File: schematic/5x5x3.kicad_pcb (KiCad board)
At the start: 4 copper layers, 100 x 100 mm, 119 parts, among them J1 SW Debug, J2 Battery, SW11 SW, SW12 SW, SW13 SW, SW14 SW, SW21 SW, SW22 SW, SW23 SW, SW24 SW, SW25 SW, SW31 SW, SW32 SW, SW33 SW, SW34 SW, SW35 SW, SW41 SW, SW42 SW, SW43 SW, SW44 SW, SW45 SW, SW51 SW, SW52 SW, SW53 SW, SW54 SW, SW55 SW, SW6 ALPS_EC11, U1 nice_nano v2

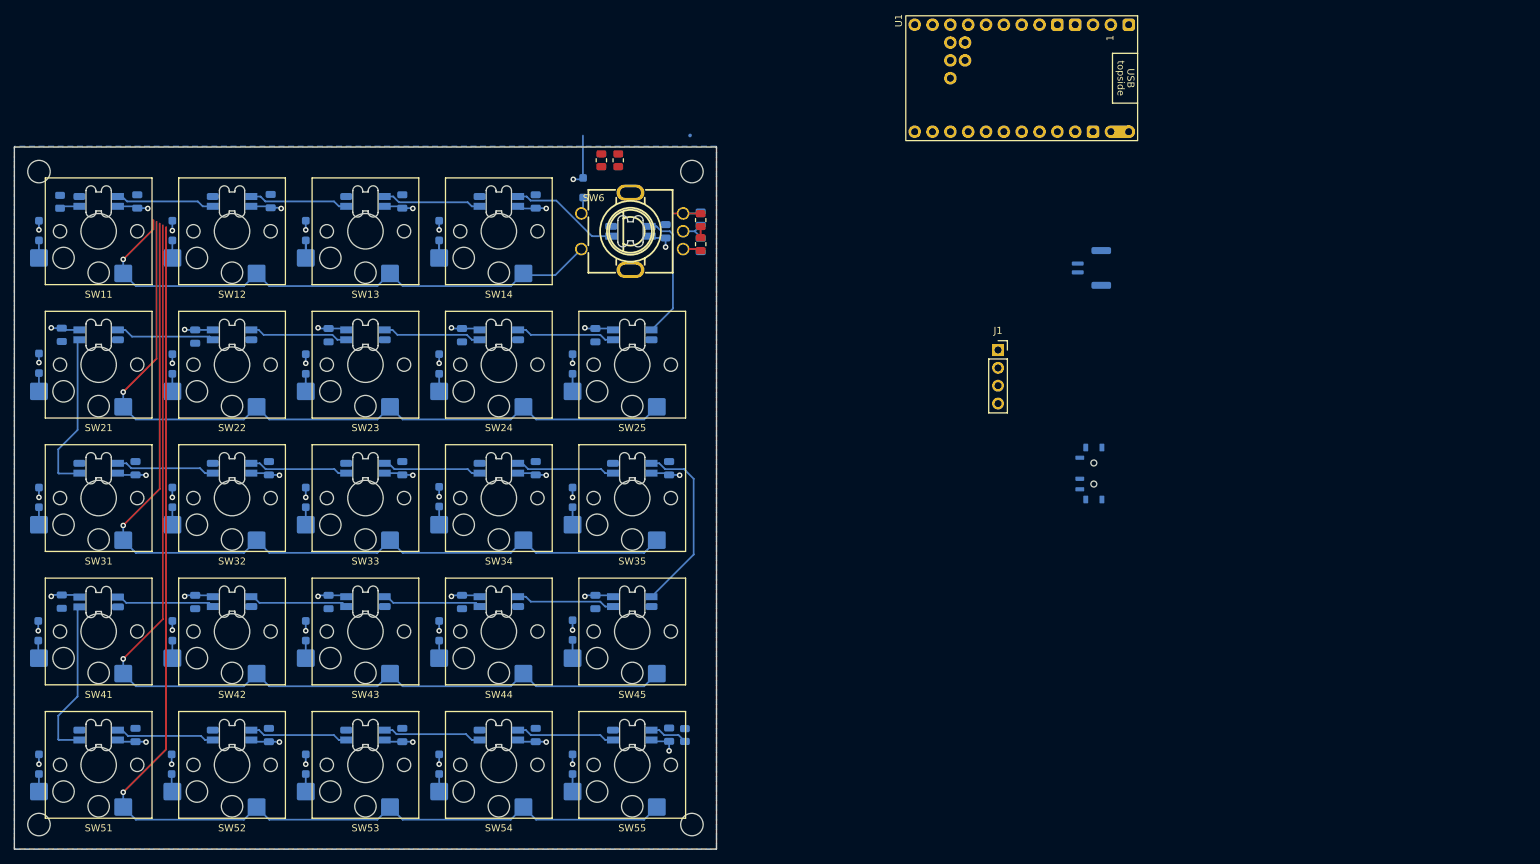
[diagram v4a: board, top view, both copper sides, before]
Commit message: Mapped 5x5x2 pins onto 5x5x3
But there is overlap, so some work is needed. Also, what rubbish am I
bringing in from the old file?
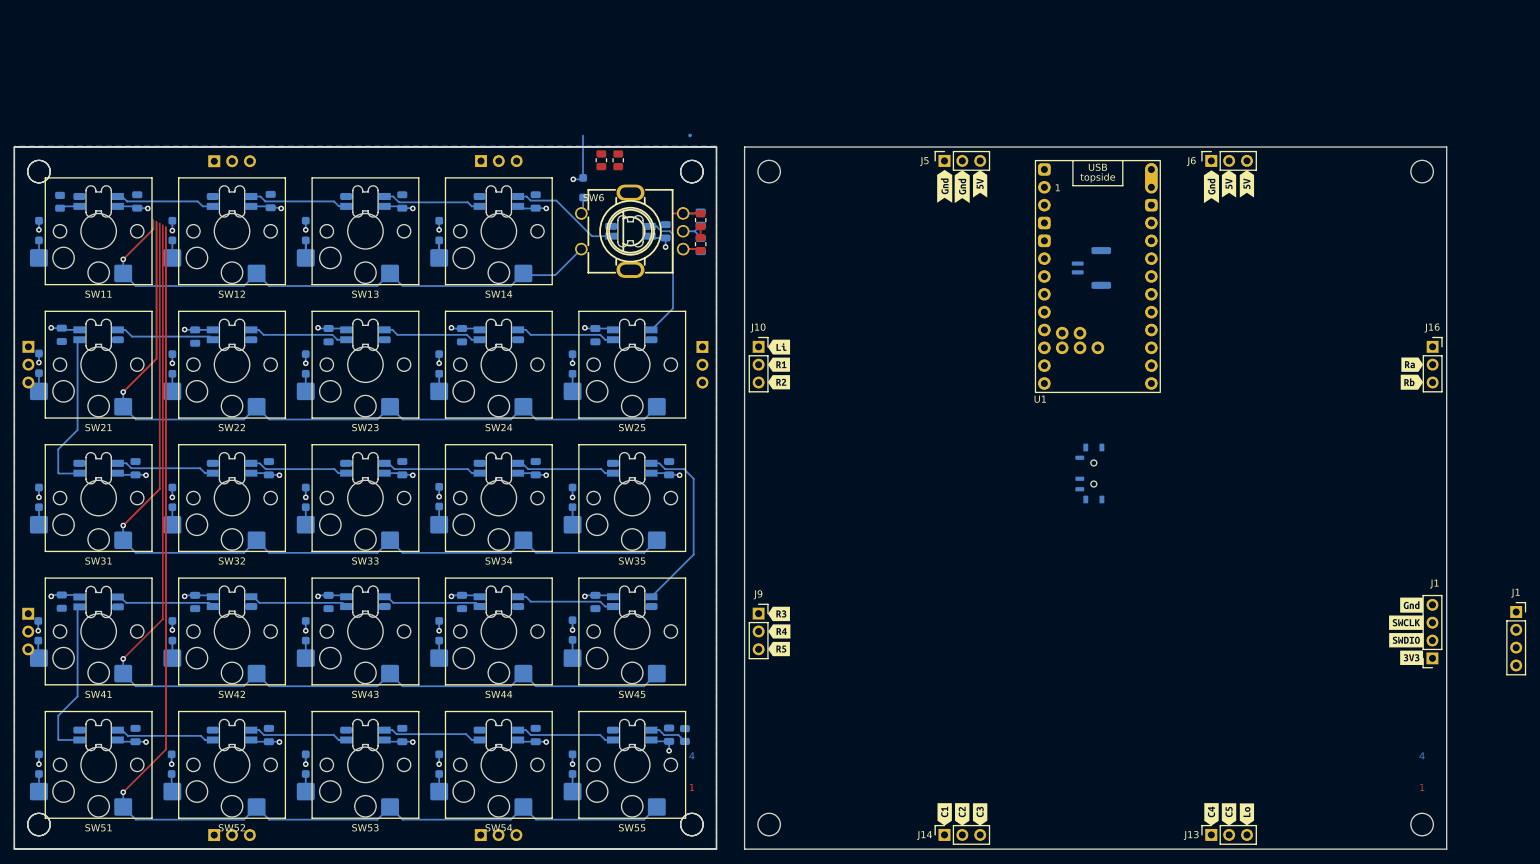
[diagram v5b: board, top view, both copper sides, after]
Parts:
- added G***: LOGO, LOGO, B.Cu at (86.0, 133.8)
- added G***: LOGO, LOGO, B.Cu at (190.0, 133.8)
- added J1: SW Debug, Connector_PinSocket_2.54mm:PinSocket_1x04_P2.54mm_Vertical, F.Cu at (238.0, 110.8)
- added J10: Conn_01x03_Female, Connector_PinSocket_2.54mm:PinSocket_1x03_P2.54mm_Vertical, F.Cu at (142.0, 66.5)
- added J11: Conn_01x03_Male, Connector_PinSocket_2.54mm:PinSocket_1x03_P2.54mm_Vertical, B.Cu at (102.4, 136.0)
- added J12: Conn_01x03_Male, Connector_PinSocket_2.54mm:PinSocket_1x03_P2.54mm_Vertical, B.Cu at (64.5, 136.0)
- added J13: Conn_01x03_Female, Connector_PinSocket_2.54mm:PinSocket_1x03_P2.54mm_Vertical, F.Cu at (206.5, 136.0)
- added J14: Conn_01x03_Female, Connector_PinSocket_2.54mm:PinSocket_1x03_P2.54mm_Vertical, F.Cu at (168.5, 136.0)
- added J15: Conn_01x03_Male, Connector_PinSocket_2.54mm:PinSocket_1x03_P2.54mm_Vertical, B.Cu at (134.0, 66.5)
- added J16: Conn_01x03_Female, Connector_PinSocket_2.54mm:PinSocket_1x03_P2.54mm_Vertical, F.Cu at (238.0, 66.5)
- added J3: Conn_01x03_Male, Connector_PinSocket_2.54mm:PinSocket_1x03_P2.54mm_Vertical, B.Cu at (64.5, 40.0)
- added J4: Conn_01x03_Male, Connector_PinSocket_2.54mm:PinSocket_1x03_P2.54mm_Vertical, B.Cu at (102.5, 40.0)
- added J5: Conn_01x03_Female, Connector_PinSocket_2.54mm:PinSocket_1x03_P2.54mm_Vertical, F.Cu at (168.5, 40.0)
- added J6: Conn_01x03_Female, Connector_PinSocket_2.54mm:PinSocket_1x03_P2.54mm_Vertical, F.Cu at (206.5, 40.0)
- added J7: Conn_01x03_Male, Connector_PinSocket_2.54mm:PinSocket_1x03_P2.54mm_Vertical, B.Cu at (38.0, 104.5)
- added J8: Conn_01x03_Male, Connector_PinSocket_2.54mm:PinSocket_1x03_P2.54mm_Vertical, B.Cu at (38.0, 66.5)
- added J9: Conn_01x03_Female, Connector_PinSocket_2.54mm:PinSocket_1x03_P2.54mm_Vertical, F.Cu at (142.0, 104.5)
- added REF**: MountingHole_3.2mm_M3, MountingHole:MountingHole_3.2mm_M3, F.Cu at (143.5, 41.5)
- added REF**: MountingHole_3.2mm_M3, MountingHole:MountingHole_3.2mm_M3, F.Cu at (132.5, 134.5)
- added REF**: MountingHole_3.2mm_M3, MountingHole:MountingHole_3.2mm_M3, F.Cu at (132.5, 41.5)
- added REF**: MountingHole_3.2mm_M3, MountingHole:MountingHole_3.2mm_M3, F.Cu at (39.5, 134.5)
- added REF**: MountingHole_3.2mm_M3, MountingHole:MountingHole_3.2mm_M3, F.Cu at (39.5, 41.5)
- added REF**: MountingHole_3.2mm_M3, MountingHole:MountingHole_3.2mm_M3, F.Cu at (236.5, 41.5)
- added REF**: MountingHole_3.2mm_M3, MountingHole:MountingHole_3.2mm_M3, F.Cu at (143.5, 134.5)
- added REF**: MountingHole_3.2mm_M3, MountingHole:MountingHole_3.2mm_M3, F.Cu at (236.5, 134.5)
- added kibuzzard-62AF6B0E: G***, kibuzzard-62AF6B0E, B.Cu at (38.0, 102.0)
- added kibuzzard-62AF6B38: G***, kibuzzard-62AF6B38, B.Cu at (40.5, 107.0)
- added kibuzzard-62AF6B38: G***, kibuzzard-62AF6B38, B.Cu at (145.0, 107.0)
- added kibuzzard-62AF6B7C: G***, kibuzzard-62AF6B7C, B.Cu at (145.0, 109.5)
- added kibuzzard-62AF6B7C: G***, kibuzzard-62AF6B7C, B.Cu at (40.5, 109.5)
- added kibuzzard-62AF6BA3: G***, kibuzzard-62AF6BA3, B.Cu at (145.0, 71.5)
- added kibuzzard-62AF6BA3: G***, kibuzzard-62AF6BA3, B.Cu at (40.5, 71.5)
- added kibuzzard-62AF6BAD: G***, kibuzzard-62AF6BAD, B.Cu at (145.0, 69.0)
- added kibuzzard-62AF6BAD: G***, kibuzzard-62AF6BAD, B.Cu at (40.5, 69.0)
- added kibuzzard-62AF6BF3: G***, kibuzzard-62AF6BF3, B.Cu at (38.0, 63.8)
- added kibuzzard-62AF6D1E: G***, kibuzzard-62AF6D1E, B.Cu at (72.5, 40.0)
- added kibuzzard-62AF6D1E: G***, kibuzzard-62AF6D1E, B.Cu at (110.5, 40.0)
- added kibuzzard-62AF6DB1: G***, kibuzzard-62AF6DB1, B.Cu at (99.0, 40.0)
- added kibuzzard-62AF6DB1: G***, kibuzzard-62AF6DB1, B.Cu at (61.0, 40.0)
- added kibuzzard-62AF6E15: G***, kibuzzard-62AF6E15, B.Cu at (131.5, 69.0)
- added kibuzzard-62AF6E21: G***, kibuzzard-62AF6E21, B.Cu at (131.5, 71.5)
- added kibuzzard-62AF6EB6: G***, kibuzzard-62AF6EB6, B.Cu at (99.8, 136.0)
- added kibuzzard-62AF6EDD: G***, kibuzzard-62AF6EDD, B.Cu at (62.0, 136.0)
- added kibuzzard-62AF6F00: G***, kibuzzard-62AF6F00, B.Cu at (72.2, 136.0)
- added kibuzzard-62AF6F11: G***, kibuzzard-62AF6F11, B.Cu at (110.0, 136.0)
- added kibuzzard-62AF73B1: G***, kibuzzard-62AF73B1, F.Cu at (206.5, 43.6)
- added kibuzzard-62AF73B1: G***, kibuzzard-62AF73B1, F.Cu at (171.0, 43.6)
- added kibuzzard-62AF73B1: G***, kibuzzard-62AF73B1, F.Cu at (168.5, 43.6)
- added kibuzzard-62AF73B1: G***, kibuzzard-62AF73B1, B.Cu at (206.5, 43.8)
- added kibuzzard-62AF73B1: G***, kibuzzard-62AF73B1, B.Cu at (171.0, 43.8)
- added kibuzzard-62AF73B1: G***, kibuzzard-62AF73B1, B.Cu at (168.5, 43.8)
- added kibuzzard-62AF73D1: G***, kibuzzard-62AF73D1, F.Cu at (209.0, 43.2)
- added kibuzzard-62AF73D1: G***, kibuzzard-62AF73D1, F.Cu at (173.6, 43.2)
- added kibuzzard-62AF73D1: G***, kibuzzard-62AF73D1, F.Cu at (211.6, 43.2)
- added kibuzzard-62AF73D1: G***, kibuzzard-62AF73D1, B.Cu at (173.5, 43.2)
- added kibuzzard-62AF73D1: G***, kibuzzard-62AF73D1, B.Cu at (209.0, 43.2)
- added kibuzzard-62AF73D1: G***, kibuzzard-62AF73D1, B.Cu at (211.5, 43.2)
- added kibuzzard-62AF7423: G***, kibuzzard-62AF7423, F.Cu at (235.1, 69.0)
- added kibuzzard-62AF742E: G***, kibuzzard-62AF742E, F.Cu at (235.1, 71.5)
- added kibuzzard-62AF7487: G***, kibuzzard-62AF7487, F.Cu at (206.5, 133.1)
- added kibuzzard-62AF7487: G***, kibuzzard-62AF7487, B.Cu at (206.5, 133.0)
- added kibuzzard-62AF7492: G***, kibuzzard-62AF7492, F.Cu at (209.0, 133.1)
- added kibuzzard-62AF7492: G***, kibuzzard-62AF7492, B.Cu at (209.0, 133.0)
- added kibuzzard-62AF749F: G***, kibuzzard-62AF749F, F.Cu at (211.6, 133.1)
- added kibuzzard-62AF749F: G***, kibuzzard-62AF749F, B.Cu at (211.5, 133.0)
- added kibuzzard-62AF74B5: G***, kibuzzard-62AF74B5, F.Cu at (168.5, 133.1)
- added kibuzzard-62AF74B5: G***, kibuzzard-62AF74B5, B.Cu at (168.5, 133.0)
- added kibuzzard-62AF74BF: G***, kibuzzard-62AF74BF, F.Cu at (171.0, 133.1)
- added kibuzzard-62AF74BF: G***, kibuzzard-62AF74BF, B.Cu at (171.0, 133.0)
- added kibuzzard-62AF74C8: G***, kibuzzard-62AF74C8, F.Cu at (173.6, 133.1)
- added kibuzzard-62AF74C8: G***, kibuzzard-62AF74C8, B.Cu at (173.5, 133.0)
- added kibuzzard-62AF74DA: G***, kibuzzard-62AF74DA, F.Cu at (144.9, 104.5)
- added kibuzzard-62AF74E3: G***, kibuzzard-62AF74E3, F.Cu at (144.9, 107.0)
- added kibuzzard-62AF74EC: G***, kibuzzard-62AF74EC, F.Cu at (144.9, 109.5)
- added kibuzzard-62AF74F7: G***, kibuzzard-62AF74F7, F.Cu at (144.9, 71.5)
- added kibuzzard-62AF74FE: G***, kibuzzard-62AF74FE, F.Cu at (144.9, 69.0)
- added kibuzzard-62AF750A: G***, kibuzzard-62AF750A, F.Cu at (144.9, 66.5)
- added kibuzzard-62AF7A14: G***, kibuzzard-62AF7A14, F.Cu at (235.0, 103.2)
- added kibuzzard-62AF7A14: G***, kibuzzard-62AF7A14, B.Cu at (235.0, 103.2)
- added kibuzzard-62AF7A28: G***, kibuzzard-62AF7A28, F.Cu at (234.2, 105.8)
- added kibuzzard-62AF7A28: G***, kibuzzard-62AF7A28, B.Cu at (234.2, 105.8)
- added kibuzzard-62AF7A49: G***, kibuzzard-62AF7A49, F.Cu at (234.2, 108.2)
- added kibuzzard-62AF7A49: G***, kibuzzard-62AF7A49, B.Cu at (234.2, 108.2)
- added kibuzzard-62AF7A56: G***, kibuzzard-62AF7A56, F.Cu at (235.0, 110.8)
- added kibuzzard-62AF7A56: G***, kibuzzard-62AF7A56, B.Cu at (235.0, 110.8)
- added kibuzzard-62AF7CA9: G***, kibuzzard-62AF7CA9, B.Cu at (145.0, 104.5)
- added kibuzzard-62AF7CCF: G***, kibuzzard-62AF7CCF, B.Cu at (145.0, 66.5)
- added kibuzzard-62B6DFF3: G***, kibuzzard-62B6DFF3, B.Cu at (235.0, 69.0)
- added kibuzzard-62B6E005: G***, kibuzzard-62B6E005, B.Cu at (235.0, 71.5)
- moved J1 82.7 mm to (249.9, 104.2)
- moved U1 31.9 mm to (190.3, 57.7), turned to 0 degrees
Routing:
- net COL2: track 139.3 -> 97.4 mm
- net COL1: track 155.9 -> 113.9 mm
- net COL3: track 122.9 -> 96.3 mm
- net COL5: track 96.7 -> 111.5 mm
- net COL4: track 106.4 -> 95.5 mm
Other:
- board size 100 x 100 mm -> 204 x 100 mm
- board text added: "1"
- board text added: "2"
- board text added: "3"
- board text added: "4"
- board text added: "Keyboard switch board connector layout"
- board text added: "MCU board connector layout"

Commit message: Routed cols and rows
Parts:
- moved D41 16.0 mm to (55.0, 110.5)
- moved D21 15.9 mm to (55.0, 72.5)
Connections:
- J3 pad 3: Vusb -> Vext
- SW21 pad 1: ROW2 -> Net-(D21-A)
- SW21 pad 2: Net-(D21-A) -> ROW2
- SW41 pad 1: ROW4 -> Net-(D41-A)
- SW41 pad 2: Net-(D41-A) -> ROW4
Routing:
- net ROW5: track 167.1 -> 112.6 mm
- net ROW4: track 148.2 -> 104.1 mm
- net COL1: track 113.9 -> 147.7 mm
- net BACKLIGHTOUT: track 0.00 -> 30.3 mm, vias 0 -> 1
- net ROW3: track 129.2 -> 102.1 mm
- net BACKLIGHTIN: track 0.00 -> 24.7 mm, vias 0 -> 1
- net ROW2: track 110.3 -> 96.9 mm
- net ROTD: track 80.7 -> 90.8 mm
- net Net-(D41-A): track 2.54 -> 3.96 mm
- net Net-(D21-A): track 2.60 -> 3.81 mm
- removed copper zone on In1.Cu, net Vext
